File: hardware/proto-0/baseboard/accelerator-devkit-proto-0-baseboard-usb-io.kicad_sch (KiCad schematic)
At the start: 36 parts, among them J2 USB-C, U10 93LC56BT-E/MNY, U2 FT2232H-56Q, U9 TPD4E05U06, X2 DSC6003HI2A-012

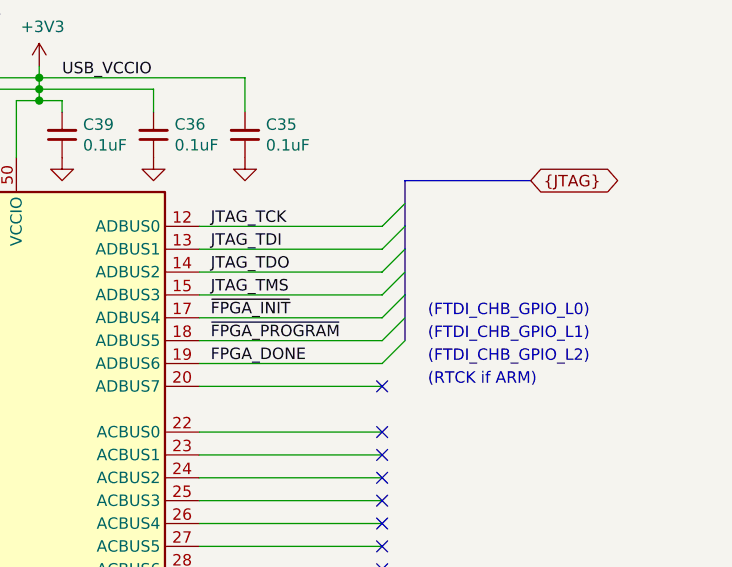
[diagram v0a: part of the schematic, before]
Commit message: Removing unused MP Pin on Qwiic connector
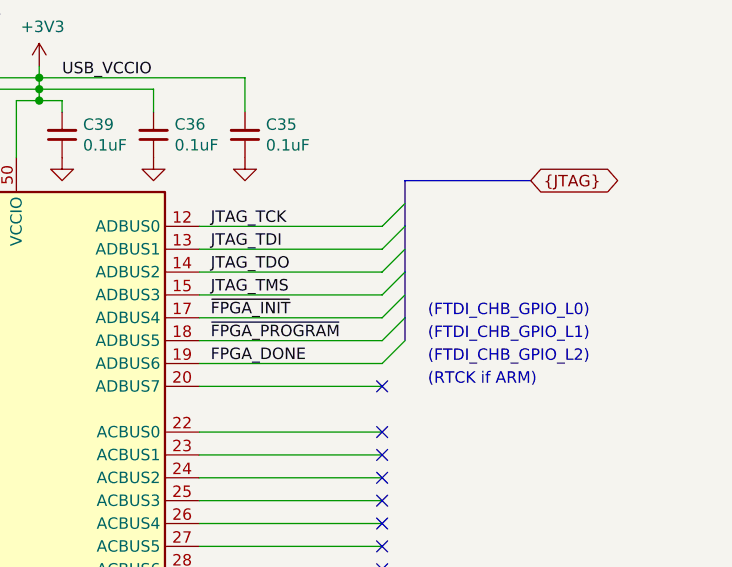
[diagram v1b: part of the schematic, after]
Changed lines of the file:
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@@
     (rev "r0")
   )
+  (bus_alias "FTDI_FIFO" (members "~FTDI_FIFO_CS" "FTDI_FIFO_A0" "~FTDI_FIFO_RD" "~FTDI_FIFO_WR" "FTDI_FIFO_DATA0" "FTDI_FIFO_DATA1" "FTDI_FIFO_DATA2" "FTDI_FIFO_DATA3" "FTDI_FIFO_DATA4" "FTDI_FIFO_DATA5" "FTDI_FIFO_DATA6" "FTDI_FIFO_DATA7"))
   (bus_alias "JTAG" (members "JTAG_TCK" "JTAG_TDI" "JTAG_TDO" "JTAG_TMS" "~FPGA_INIT" "~FPGA_PROGRAM" "FPGA_DONE"))
   (bus_alias "FTDI_SPI" (members "FTDI_SPI_SCLK" "FTDI_SPI_MOSI" "FTDI_SPI_MISO" "FTDI_SPI_CS"))
-  (bus_alias "FTDI_FIFO" (members "~FTDI_FIFO_CS" "FTDI_FIFO_A0" "~FTDI_FIFO_RD" "~FTDI_FIFO_WR" "FTDI_FIFO_DATA0" "FTDI_FIFO_DATA1" "FTDI_FIFO_DATA2" "FTDI_FIFO_DATA3" "FTDI_FIFO_DATA4" "FTDI_FIFO_DATA5" "FTDI_FIFO_DATA6" "FTDI_FIFO_DATA7"))
   (junction (at 19.05 99.06))
   (junction (at 19.05 106.68))
@@
   (junction (at 204.47 62.23))
   (junction (at 204.47 63.5))
+  (no_connect (at 41.91 54.61))
+  (no_connect (at 242.57 107.95))
+  (no_connect (at 242.57 153.67))
+  (no_connect (at 242.57 161.29))
+  (no_connect (at 41.91 62.23))
+  (no_connect (at 242.57 110.49))
+  (no_connect (at 41.91 77.47))
+  (no_connect (at 242.57 95.25))
+  (no_connect (at 242.57 158.75))
+  (no_connect (at 242.57 100.33))
+  (no_connect (at 222.25 171.45))
+  (no_connect (at 41.91 69.85))
+  (no_connect (at 242.57 113.03))
+  (no_connect (at 41.91 59.69))
+  (no_connect (at 242.57 105.41))
+  (no_connect (at 242.57 163.83))
+  (no_connect (at 41.91 74.93))
+  (no_connect (at 242.57 146.05))
+  (no_connect (at 242.57 115.57))
+  (no_connect (at 242.57 148.59))
+  (no_connect (at 242.57 156.21))
   (no_connect (at 124.46 179.07))
-  (no_connect (at 41.91 69.85))
-  (no_connect (at 242.57 105.41))
-  (no_connect (at 41.91 62.23))
-  (no_connect (at 41.91 59.69))
-  (no_connect (at 242.57 95.25))
-  (no_connect (at 242.57 115.57))
-  (no_connect (at 242.57 100.33))
+  (no_connect (at 41.91 52.07))
+  (no_connect (at 242.57 118.11))
+  (no_connect (at 161.29 166.37))
+  (no_connect (at 222.25 168.91))
   (no_connect (at 41.91 67.31))
-  (no_connect (at 242.57 110.49))
-  (no_connect (at 222.25 168.91))
-  (no_connect (at 242.57 113.03))
-  (no_connect (at 242.57 118.11))
-  (no_connect (at 242.57 158.75))
-  (no_connect (at 242.57 163.83))
-  (no_connect (at 242.57 107.95))
-  (no_connect (at 242.57 161.29))
+  (no_connect (at 41.91 44.45))
+  (no_connect (at 242.57 102.87))
+  (no_connect (at 41.91 46.99))
   (no_connect (at 242.57 151.13))
-  (no_connect (at 41.91 46.99))
-  (no_connect (at 242.57 153.67))
-  (no_connect (at 41.91 44.45))
-  (no_connect (at 41.91 77.47))
-  (no_connect (at 242.57 146.05))
-  (no_connect (at 242.57 102.87))
-  (no_connect (at 222.25 171.45))
-  (no_connect (at 41.91 74.93))
-  (no_connect (at 161.29 166.37))
-  (no_connect (at 41.91 52.07))
-  (no_connect (at 242.57 148.59))
-  (no_connect (at 41.91 54.61))
-  (no_connect (at 242.57 156.21))
   (bus_entry (at 242.57 77.47) (size 2.54 -2.54))
   (bus_entry (at 242.57 80.01) (size 2.54 -2.54))
@@
     (stroke (width 0) (type solid) (color 0 0 0 0))
   )
-  (bus (pts (xy 245.11 77.47) (xy 245.11 80.01))
-    (stroke (width 0) (type solid) (color 0 0 0 0))
-  )
-  (bus (pts (xy 245.11 80.01) (xy 245.11 85.09))
-    (stroke (width 0) (type solid) (color 0 0 0 0))
-  )
-  (bus (pts (xy 245.11 85.09) (xy 245.11 90.17))
-    (stroke (width 0) (type solid) (color 0 0 0 0))
-  )
+  (bus (pts (xy 245.11 77.47) (xy 245.11 82.55))
+    (stroke (width 0) (type solid) (color 0 0 0 0))
+  )
+  (bus (pts (xy 245.11 82.55) (xy 245.11 87.63))
+    (stroke (width 0) (type solid) (color 0 0 0 0))
+  )
+  (bus (pts (xy 245.11 87.63) (xy 245.11 90.17))
+    (stroke (width 0) (type solid) (color 0 0 0 0))
+  )

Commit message: Moving all power rail test points to the front
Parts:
- TP6: footprint TestPoint:TestPoint_Pad_D1.0mm -> TestPoint:TestPoint_THTPad_D1.0mm_Drill0.5mm
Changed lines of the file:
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@@
     (rev "r0")
   )
+  (bus_alias "FTDI_SPI" (members "FTDI_SPI_SCLK" "FTDI_SPI_MOSI" "FTDI_SPI_MISO" "FTDI_SPI_CS"))
   (bus_alias "FTDI_FIFO" (members "~FTDI_FIFO_CS" "FTDI_FIFO_A0" "~FTDI_FIFO_RD" "~FTDI_FIFO_WR" "FTDI_FIFO_DATA0" "FTDI_FIFO_DATA1" "FTDI_FIFO_DATA2" "FTDI_FIFO_DATA3" "FTDI_FIFO_DATA4" "FTDI_FIFO_DATA5" "FTDI_FIFO_DATA6" "FTDI_FIFO_DATA7"))
   (bus_alias "JTAG" (members "JTAG_TCK" "JTAG_TDI" "JTAG_TDO" "JTAG_TMS" "~FPGA_INIT" "~FPGA_PROGRAM" "FPGA_DONE"))
-  (bus_alias "FTDI_SPI" (members "FTDI_SPI_SCLK" "FTDI_SPI_MOSI" "FTDI_SPI_MISO" "FTDI_SPI_CS"))
   (junction (at 19.05 99.06))
   (junction (at 19.05 106.68))
@@
   (junction (at 204.47 62.23))
   (junction (at 204.47 63.5))
-  (no_connect (at 41.91 54.61))
-  (no_connect (at 242.57 107.95))
-  (no_connect (at 242.57 153.67))
-  (no_connect (at 242.57 161.29))
-  (no_connect (at 41.91 62.23))
+  (no_connect (at 242.57 151.13))
   (no_connect (at 242.57 110.49))
-  (no_connect (at 41.91 77.47))
-  (no_connect (at 242.57 95.25))
-  (no_connect (at 242.57 158.75))
-  (no_connect (at 242.57 100.33))
-  (no_connect (at 222.25 171.45))
-  (no_connect (at 41.91 69.85))
-  (no_connect (at 242.57 113.03))
-  (no_connect (at 41.91 59.69))
-  (no_connect (at 242.57 105.41))
+  (no_connect (at 242.57 102.87))
+  (no_connect (at 242.57 156.21))
   (no_connect (at 242.57 163.83))
   (no_connect (at 41.91 74.93))
+  (no_connect (at 242.57 148.59))
+  (no_connect (at 41.91 77.47))
+  (no_connect (at 242.57 115.57))
+  (no_connect (at 242.57 158.75))
+  (no_connect (at 242.57 161.29))
+  (no_connect (at 242.57 105.41))
+  (no_connect (at 41.91 54.61))
+  (no_connect (at 242.57 113.03))
+  (no_connect (at 242.57 118.11))
+  (no_connect (at 41.91 44.45))
+  (no_connect (at 41.91 46.99))
+  (no_connect (at 124.46 179.07))
+  (no_connect (at 41.91 67.31))
+  (no_connect (at 222.25 168.91))
+  (no_connect (at 242.57 95.25))
   (no_connect (at 242.57 146.05))
-  (no_connect (at 242.57 115.57))
-  (no_connect (at 242.57 148.59))
-  (no_connect (at 242.57 156.21))
-  (no_connect (at 124.46 179.07))
+  (no_connect (at 41.91 69.85))
+  (no_connect (at 242.57 153.67))
+  (no_connect (at 242.57 107.95))
+  (no_connect (at 242.57 100.33))
+  (no_connect (at 41.91 62.23))
+  (no_connect (at 41.91 59.69))
+  (no_connect (at 222.25 171.45))
   (no_connect (at 41.91 52.07))
-  (no_connect (at 242.57 118.11))
   (no_connect (at 161.29 166.37))
-  (no_connect (at 222.25 168.91))
-  (no_connect (at 41.91 67.31))
-  (no_connect (at 41.91 44.45))
-  (no_connect (at 242.57 102.87))
-  (no_connect (at 41.91 46.99))
-  (no_connect (at 242.57 151.13))
   (bus_entry (at 242.57 77.47) (size 2.54 -2.54))
   (bus_entry (at 242.57 80.01) (size 2.54 -2.54))
@@
       (effects (font (size 1.27 1.27)) (justify left) hide)
     )
-    (property "Footprint" "TestPoint:TestPoint_Pad_D1.0mm" (id 2) (at 91.44 24.13 0)
+    (property "Footprint" "TestPoint:TestPoint_THTPad_D1.0mm_Drill0.5mm" (id 2) (at 91.44 24.13 0)
       (effects (font (size 1.27 1.27)) hide)
     )

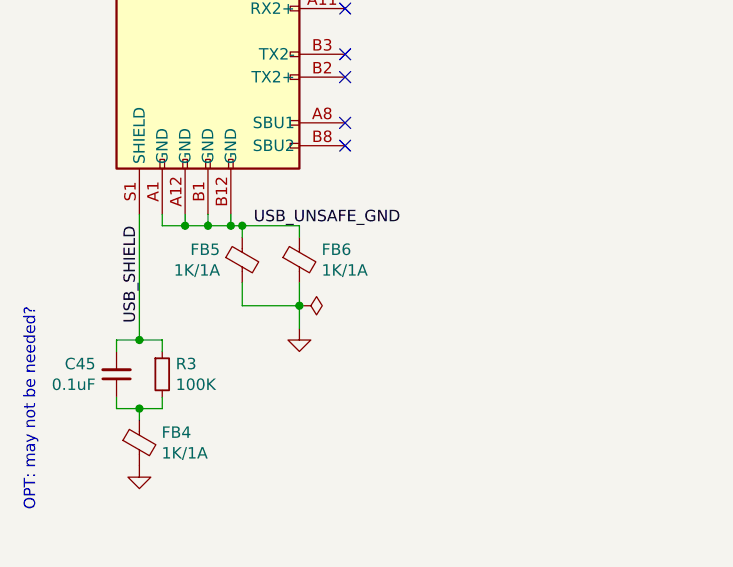
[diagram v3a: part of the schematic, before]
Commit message: Switching USB connector to CUI UJ31-CH-3-MSMT-TR-67
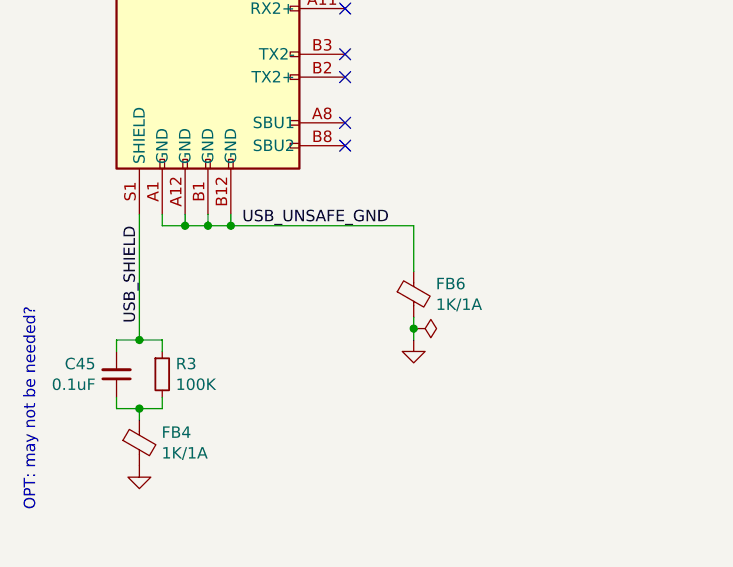
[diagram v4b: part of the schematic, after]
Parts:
- removed FB5: 1K/1A, Inductor_SMD:L_0805_2012Metric, symbol Device:Ferrite_Bead_Small
- J2: footprint Connector_USB_RD:JAE_DX07B024JJ1R1500 -> Connector_USB_RD:CUI_UJ31-CH-3-MSMT-TR-67
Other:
- moved on the sheet: FB6
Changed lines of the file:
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@@
     (rev "r0")
   )
+  (bus_alias "JTAG" (members "JTAG_TCK" "JTAG_TDI" "JTAG_TDO" "JTAG_TMS" "~FPGA_INIT" "~FPGA_PROGRAM" "FPGA_DONE"))
   (bus_alias "FTDI_SPI" (members "FTDI_SPI_SCLK" "FTDI_SPI_MOSI" "FTDI_SPI_MISO" "FTDI_SPI_CS"))
   (bus_alias "FTDI_FIFO" (members "~FTDI_FIFO_CS" "FTDI_FIFO_A0" "~FTDI_FIFO_RD" "~FTDI_FIFO_WR" "FTDI_FIFO_DATA0" "FTDI_FIFO_DATA1" "FTDI_FIFO_DATA2" "FTDI_FIFO_DATA3" "FTDI_FIFO_DATA4" "FTDI_FIFO_DATA5" "FTDI_FIFO_DATA6" "FTDI_FIFO_DATA7"))
-  (bus_alias "JTAG" (members "JTAG_TCK" "JTAG_TDI" "JTAG_TDO" "JTAG_TMS" "~FPGA_INIT" "~FPGA_PROGRAM" "FPGA_DONE"))
   (junction (at 19.05 99.06))
   (junction (at 19.05 106.68))
@@
   (junction (at 26.67 86.36))
   (junction (at 29.21 86.36))
-  (junction (at 30.48 86.36))
-  (junction (at 36.83 95.25))
   (junction (at 43.18 33.02))
   (junction (at 43.18 38.1))
+  (junction (at 49.53 97.79))
   (junction (at 54.61 38.1))
   (junction (at 57.15 46.99))
@@
   (junction (at 204.47 62.23))
   (junction (at 204.47 63.5))
-  (no_connect (at 242.57 151.13))
-  (no_connect (at 242.57 110.49))
-  (no_connect (at 242.57 102.87))
+  (no_connect (at 242.57 95.25))
+  (no_connect (at 41.91 59.69))
+  (no_connect (at 242.57 113.03))
+  (no_connect (at 242.57 158.75))
+  (no_connect (at 242.57 148.59))
+  (no_connect (at 222.25 168.91))
   (no_connect (at 242.57 156.21))
-  (no_connect (at 242.57 163.83))
-  (no_connect (at 41.91 74.93))
-  (no_connect (at 242.57 148.59))
-  (no_connect (at 41.91 77.47))
-  (no_connect (at 242.57 115.57))
-  (no_connect (at 242.57 158.75))
-  (no_connect (at 242.57 161.29))
-  (no_connect (at 242.57 105.41))
-  (no_connect (at 41.91 54.61))
-  (no_connect (at 242.57 113.03))
-  (no_connect (at 242.57 118.11))
-  (no_connect (at 41.91 44.45))
+  (no_connect (at 242.57 107.95))
   (no_connect (at 41.91 46.99))
   (no_connect (at 124.46 179.07))
+  (no_connect (at 161.29 166.37))
+  (no_connect (at 41.91 44.45))
+  (no_connect (at 242.57 118.11))
+  (no_connect (at 242.57 163.83))
+  (no_connect (at 41.91 54.61))
+  (no_connect (at 41.91 69.85))
+  (no_connect (at 41.91 62.23))
+  (no_connect (at 242.57 146.05))
+  (no_connect (at 41.91 74.93))
   (no_connect (at 41.91 67.31))
-  (no_connect (at 222.25 168.91))
-  (no_connect (at 242.57 95.25))
-  (no_connect (at 242.57 146.05))
-  (no_connect (at 41.91 69.85))
+  (no_connect (at 242.57 110.49))
+  (no_connect (at 242.57 105.41))
   (no_connect (at 242.57 153.67))
-  (no_connect (at 242.57 107.95))
+  (no_connect (at 242.57 151.13))
+  (no_connect (at 242.57 102.87))
+  (no_connect (at 41.91 77.47))
   (no_connect (at 242.57 100.33))
-  (no_connect (at 41.91 62.23))
-  (no_connect (at 41.91 59.69))
+  (no_connect (at 242.57 115.57))
+  (no_connect (at 242.57 161.29))
   (no_connect (at 222.25 171.45))
   (no_connect (at 41.91 52.07))
-  (no_connect (at 161.29 166.37))
   (bus_entry (at 242.57 77.47) (size 2.54 -2.54))
   (bus_entry (at 242.57 80.01) (size 2.54 -2.54))
@@
     (stroke (width 0) (type solid) (color 0 0 0 0))
   )
+  (wire (pts (xy 21.59 86.36) (xy 24.13 86.36))
+    (stroke (width 0) (type solid) (color 0 0 0 0))
+  )
   (wire (pts (xy 21.59 99.06) (xy 21.59 100.33))
     (stroke (width 0) (type solid) (color 0 0 0 0))
@@
     (stroke (width 0) (type solid) (color 0 0 0 0))
   )
-  (wire (pts (xy 24.13 86.36) (xy 21.59 86.36))
-    (stroke (width 0) (type solid) (color 0 0 0 0))
-  )
   (wire (pts (xy 24.13 86.36) (xy 26.67 86.36))
     (stroke (width 0) (type solid) (color 0 0 0 0))
@@
     (stroke (width 0) (type solid) (color 0 0 0 0))
   )
-  (wire (pts (xy 29.21 86.36) (xy 30.48 86.36))
-    (stroke (width 0) (type solid) (color 0 0 0 0))
-  )
-  (wire (pts (xy 30.48 86.36) (xy 30.48 87.63))
-    (stroke (width 0) (type solid) (color 0 0 0 0))
-  )
-  (wire (pts (xy 30.48 86.36) (xy 36.83 86.36))
-    (stroke (width 0) (type solid) (color 0 0 0 0))
-  )
-  (wire (pts (xy 30.48 92.71) (xy 30.48 95.25))
-    (stroke (width 0) (type solid) (color 0 0 0 0))
-  )
-  (wire (pts (xy 30.48 95.25) (xy 36.83 95.25))
-    (stroke (width 0) (type solid) (color 0 0 0 0))
-  )
-  (wire (pts (xy 36.83 86.36) (xy 36.83 87.63))
-    (stroke (width 0) (type solid) (color 0 0 0 0))
-  )
-  (wire (pts (xy 36.83 95.25) (xy 36.83 92.71))
-    (stroke (width 0) (type solid) (color 0 0 0 0))
-  )
-  (wire (pts (xy 36.83 95.25) (xy 36.83 97.79))
+  (wire (pts (xy 29.21 86.36) (xy 49.53 86.36))
     (stroke (width 0) (type solid) (color 0 0 0 0))
   )
@@
   )
   (wire (pts (xy 45.72 139.7) (xy 55.88 139.7))
+    (stroke (width 0) (type solid) (color 0 0 0 0))
+  )
+  (wire (pts (xy 49.53 86.36) (xy 49.53 91.44))
+    (stroke (width 0) (type solid) (color 0 0 0 0))
+  )
+  (wire (pts (xy 49.53 97.79) (xy 49.53 96.52))
+    (stroke (width 0) (type solid) (color 0 0 0 0))
+  )
+  (wire (pts (xy 49.53 97.79) (xy 49.53 99.06))
     (stroke (width 0) (type solid) (color 0 0 0 0))
   )
@@
     (effects (font (size 1.27 1.27)) (justify right bottom))
   )
-  (label "USB_UNSAFE_GND" (at 31.75 86.36 0)
+  (label "USB_UNSAFE_GND" (at 30.48 86.36 0)
     (effects (font (size 1.27 1.27)) (justify left bottom))
   )
@@
     )
   )
-  (symbol (lib_id "power:PWR_FLAG") (at 36.83 95.25 270) (unit 1)
-    (property "Reference" "#FLG0101" (id 0) (at 38.735 95.25 0)
-      (effects (font (size 1.27 1.27)) hide)
-    )
-    (property "Value" "PWR_FLAG" (id 1) (at 40.005 95.25 90)
+  (symbol (lib_id "power:PWR_FLAG") (at 49.53 97.79 270) (unit 1)
+    (property "Reference" "#FLG0101" (id 0) (at 51.435 97.79 0)
+      (effects (font (size 1.27 1.27)) hide)
+    )
+    (property "Value" "PWR_FLAG" (id 1) (at 52.705 97.79 90)
       (effects (font (size 1.27 1.27)) (justify left) hide)
     )
-    (property "Footprint" "" (id 2) (at 36.83 95.25 0)
-      (effects (font (size 1.27 1.27)) hide)
-    )
-    (property "Datasheet" "~" (id 3) (at 36.83 95.25 0)
+    (property "Footprint" "" (id 2) (at 49.53 97.79 0)
+      (effects (font (size 1.27 1.27)) hide)
+    )
+    (property "Datasheet" "~" (id 3) (at 49.53 97.79 0)
       (effects (font (size 1.27 1.27)) hide)
     )
@@
     )
   )
-  (symbol (lib_id "power:GND") (at 36.83 97.79 0) (unit 1)
-    (property "Reference" "#PWR044" (id 0) (at 36.83 104.14 0)
-      (effects (font (size 1.27 1.27)) hide)
-    )
-    (property "Value" "GND" (id 1) (at 36.957 102.1842 0)
-      (effects (font (size 1.27 1.27)) hide)
-    )
-    (property "Footprint" "" (id 2) (at 36.83 97.79 0)
-      (effects (font (size 1.27 1.27)) hide)
-    )
-    (property "Datasheet" "" (id 3) (at 36.83 97.79 0)
+  (symbol (lib_id "power:GND") (at 49.53 99.06 0) (unit 1)
+    (property "Reference" "#PWR0103" (id 0) (at 49.53 105.41 0)
+      (effects (font (size 1.27 1.27)) hide)
+    )
+    (property "Value" "GND" (id 1) (at 49.657 103.4542 0)
+      (effects (font (size 1.27 1.27)) hide)
+    )
+    (property "Footprint" "" (id 2) (at 49.53 99.06 0)
+      (effects (font (size 1.27 1.27)) hide)
+    )
+    (property "Datasheet" "" (id 3) (at 49.53 99.06 0)
       (effects (font (size 1.27 1.27)) hide)
     )
@@
     )
   )
-  (symbol (lib_id "Device:Ferrite_Bead_Small") (at 30.48 90.17 0) (unit 1)
-    (property "Reference" "FB5" (id 0) (at 28.0162 89.0206 0)
-      (effects (font (size 1.27 1.27)) (justify right))
-    )
-    (property "Value" "1K/1A" (id 1) (at 28.0162 91.3193 0)
-      (effects (font (size 1.27 1.27)) (justify right))
-    )
-    (property "Footprint" "Inductor_SMD:L_0805_2012Metric" (id 2) (at 28.702 90.17 90)
-      (effects (font (size 1.27 1.27)) hide)
-    )
-    (property "Datasheet" "https://www.murata.com/en-us/api/pdfdownloadapi?cate=luNoiseSupprFilteChipImpNFZ&partno=NFZ2MSD102SZ10%23" (id 3) (at 30.48 90.17 0)
-      (effects (font (size 1.27 1.27)) hide)
-    )
-    (property "Part" "NFZ2MSD102SZ10L" (id 4) (at 30.48 90.17 0)
-      (effects (font (size 1.27 1.27)) hide)
-    )
-  )
-  (symbol (lib_id "Device:Ferrite_Bead_Small") (at 36.83 90.17 0) (unit 1)
-    (property "Reference" "FB6" (id 0) (at 39.2939 89.0206 0)
-      (effects (font (size 1.27 1.27)) (justify left))
-    )
-    (property "Value" "1K/1A" (id 1) (at 39.2939 91.3193 0)
-      (effects (font (size 1.27 1.27)) (justify left))
-    )
-    (property "Footprint" "Inductor_SMD:L_0805_2012Metric" (id 2) (at 35.052 90.17 90)
-      (effects (font (size 1.27 1.27)) hide)
-    )
-    (property "Datasheet" "https://www.murata.com/en-us/api/pdfdownloadapi?cate=luNoiseSupprFilteChipImpNFZ&partno=NFZ2MSD102SZ10%23" (id 3) (at 36.83 90.17 0)
-      (effects (font (size 1.27 1.27)) hide)
-    )
-    (property "Part" "NFZ2MSD102SZ10L" (id 4) (at 36.83 90.17 0)
+  (symbol (lib_id "Device:Ferrite_Bead_Small") (at 49.53 93.98 0) (unit 1)
+    (property "Reference" "FB6" (id 0) (at 51.9939 92.8306 0)
+      (effects (font (size 1.27 1.27)) (justify left))
+    )
+    (property "Value" "1K/1A" (id 1) (at 51.9939 95.1293 0)
+      (effects (font (size 1.27 1.27)) (justify left))
+    )
+    (property "Footprint" "Inductor_SMD:L_0805_2012Metric" (id 2) (at 47.752 93.98 90)
+      (effects (font (size 1.27 1.27)) hide)
+    )
+    (property "Datasheet" "https://www.murata.com/en-us/api/pdfdownloadapi?cate=luNoiseSupprFilteChipImpNFZ&partno=NFZ2MSD102SZ10%23" (id 3) (at 49.53 93.98 0)
+      (effects (font (size 1.27 1.27)) hide)
+    )
+    (property "Part" "NFZ2MSD102SZ10L" (id 4) (at 49.53 93.98 0)
       (effects (font (size 1.27 1.27)) hide)
     )
@@
     (property "Reference" "J2" (id 0) (at 29.388 12.268 0))
     (property "Value" "USB-C" (id 1) (at 29.3878 14.5796 0))
-    (property "Footprint" "Connector_USB_RD:JAE_DX07B024JJ1R1500" (id 2) (at 30.48 44.45 0)
-      (effects (font (size 1.27 1.27)) hide)
-    )
+    (property "Footprint" "Connector_USB_RD:CUI_UJ31-CH-3-MSMT-TR-67" (id 2) (at 30.48 44.45 0)
+      (effects (font (size 1.27 1.27)) hide)
+    )
